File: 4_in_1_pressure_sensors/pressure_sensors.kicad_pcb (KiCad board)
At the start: 4 copper layers, 100 x 100 mm, 73 parts, among them J1 Conn_02x04_Odd_Even, J2 Conn_02x07_Odd_Even, U1 ABPDANT060MGAA5, U1 ABPDJJ001PDSA3, U1 MPX5100AP, U2 LM358

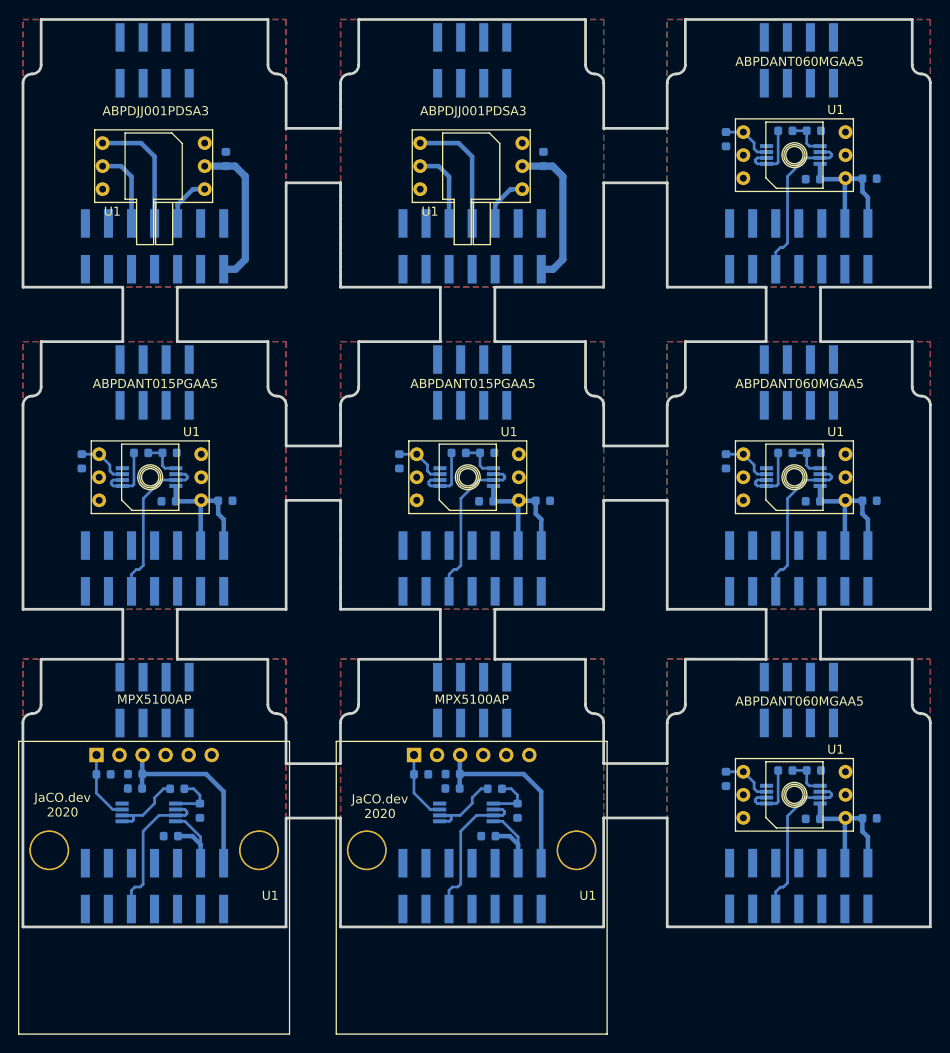
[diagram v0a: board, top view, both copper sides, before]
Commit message: Added mouse bites for pressure sensors PCB
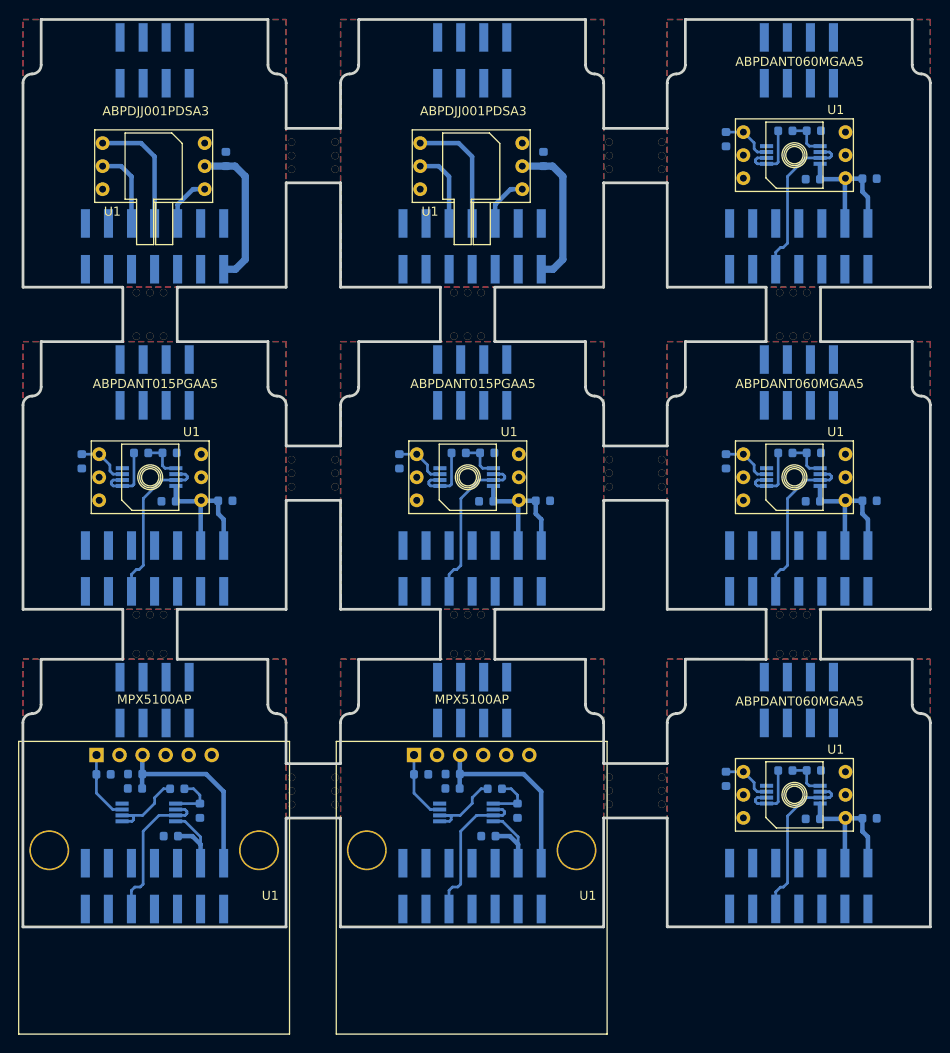
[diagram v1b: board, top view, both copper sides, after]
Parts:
- added ?: SolderWirePad_1x01_Drill0.8mm, Connector_Wire:SolderWirePad_1x01_Drill0.8mm, F.Cu at (204.6, 125.0)
- added ?: SolderWirePad_1x01_Drill0.8mm, Connector_Wire:SolderWirePad_1x01_Drill0.8mm, F.Cu at (210.4, 90.0)
- added ?: SolderWirePad_1x01_Drill0.8mm, Connector_Wire:SolderWirePad_1x01_Drill0.8mm, F.Cu at (204.6, 91.5)
- added ?: SolderWirePad_1x01_Drill0.8mm, Connector_Wire:SolderWirePad_1x01_Drill0.8mm, F.Cu at (204.6, 88.5)
- added ?: SolderWirePad_1x01_Drill0.8mm, Connector_Wire:SolderWirePad_1x01_Drill0.8mm, F.Cu at (210.4, 55.0)
- added ?: SolderWirePad_1x01_Drill0.8mm, Connector_Wire:SolderWirePad_1x01_Drill0.8mm, F.Cu at (204.6, 53.5)
- added ?: SolderWirePad_1x01_Drill0.8mm, Connector_Wire:SolderWirePad_1x01_Drill0.8mm, F.Cu at (210.4, 56.5)
- added ?: SolderWirePad_1x01_Drill0.8mm, Connector_Wire:SolderWirePad_1x01_Drill0.8mm, F.Cu at (204.6, 55.0)
- added ?: SolderWirePad_1x01_Drill0.8mm, Connector_Wire:SolderWirePad_1x01_Drill0.8mm, F.Cu at (210.4, 53.5)
- added ?: SolderWirePad_1x01_Drill0.8mm, Connector_Wire:SolderWirePad_1x01_Drill0.8mm, F.Cu at (204.6, 56.5)
- added ?: SolderWirePad_1x01_Drill0.8mm, Connector_Wire:SolderWirePad_1x01_Drill0.8mm, F.Cu at (174.4, 125.0)
- added ?: SolderWirePad_1x01_Drill0.8mm, Connector_Wire:SolderWirePad_1x01_Drill0.8mm, F.Cu at (210.4, 126.5)
- added ?: SolderWirePad_1x01_Drill0.8mm, Connector_Wire:SolderWirePad_1x01_Drill0.8mm, F.Cu at (169.6, 123.5)
- added ?: SolderWirePad_1x01_Drill0.8mm, Connector_Wire:SolderWirePad_1x01_Drill0.8mm, F.Cu at (174.4, 126.5)
- added ?: SolderWirePad_1x01_Drill0.8mm, Connector_Wire:SolderWirePad_1x01_Drill0.8mm, F.Cu at (169.6, 125.0)
- added ?: SolderWirePad_1x01_Drill0.8mm, Connector_Wire:SolderWirePad_1x01_Drill0.8mm, F.Cu at (174.4, 123.5)
- added ?: SolderWirePad_1x01_Drill0.8mm, Connector_Wire:SolderWirePad_1x01_Drill0.8mm, F.Cu at (169.6, 126.5)
- added ?: SolderWirePad_1x01_Drill0.8mm, Connector_Wire:SolderWirePad_1x01_Drill0.8mm, F.Cu at (174.4, 90.0)
- added ?: SolderWirePad_1x01_Drill0.8mm, Connector_Wire:SolderWirePad_1x01_Drill0.8mm, F.Cu at (169.6, 88.5)
- added ?: SolderWirePad_1x01_Drill0.8mm, Connector_Wire:SolderWirePad_1x01_Drill0.8mm, F.Cu at (174.4, 91.5)
- added ?: SolderWirePad_1x01_Drill0.8mm, Connector_Wire:SolderWirePad_1x01_Drill0.8mm, F.Cu at (169.6, 90.0)
- added ?: SolderWirePad_1x01_Drill0.8mm, Connector_Wire:SolderWirePad_1x01_Drill0.8mm, F.Cu at (174.4, 88.5)
- added ?: SolderWirePad_1x01_Drill0.8mm, Connector_Wire:SolderWirePad_1x01_Drill0.8mm, F.Cu at (210.4, 123.5)
- added ?: SolderWirePad_1x01_Drill0.8mm, Connector_Wire:SolderWirePad_1x01_Drill0.8mm, F.Cu at (169.6, 91.5)
- added ?: SolderWirePad_1x01_Drill0.8mm, Connector_Wire:SolderWirePad_1x01_Drill0.8mm, F.Cu at (174.4, 55.0)
- added ?: SolderWirePad_1x01_Drill0.8mm, Connector_Wire:SolderWirePad_1x01_Drill0.8mm, F.Cu at (169.6, 53.5)
- added ?: SolderWirePad_1x01_Drill0.8mm, Connector_Wire:SolderWirePad_1x01_Drill0.8mm, F.Cu at (174.4, 56.5)
- added ?: SolderWirePad_1x01_Drill0.8mm, Connector_Wire:SolderWirePad_1x01_Drill0.8mm, F.Cu at (169.6, 55.0)
- added ?: SolderWirePad_1x01_Drill0.8mm, Connector_Wire:SolderWirePad_1x01_Drill0.8mm, F.Cu at (174.4, 53.5)
- added ?: SolderWirePad_1x01_Drill0.8mm, Connector_Wire:SolderWirePad_1x01_Drill0.8mm, F.Cu at (169.6, 56.5)
- added ?: SolderWirePad_1x01_Drill0.8mm, Connector_Wire:SolderWirePad_1x01_Drill0.8mm, F.Cu at (224.9, 74.9)
- added ?: SolderWirePad_1x01_Drill0.8mm, Connector_Wire:SolderWirePad_1x01_Drill0.8mm, F.Cu at (226.4, 70.1)
- added ?: SolderWirePad_1x01_Drill0.8mm, Connector_Wire:SolderWirePad_1x01_Drill0.8mm, F.Cu at (223.4, 74.9)
- added ?: SolderWirePad_1x01_Drill0.8mm, Connector_Wire:SolderWirePad_1x01_Drill0.8mm, F.Cu at (210.4, 125.0)
- added ?: SolderWirePad_1x01_Drill0.8mm, Connector_Wire:SolderWirePad_1x01_Drill0.8mm, F.Cu at (224.9, 70.1)
- added ?: SolderWirePad_1x01_Drill0.8mm, Connector_Wire:SolderWirePad_1x01_Drill0.8mm, F.Cu at (226.4, 74.9)
- added ?: SolderWirePad_1x01_Drill0.8mm, Connector_Wire:SolderWirePad_1x01_Drill0.8mm, F.Cu at (223.4, 70.1)
- added ?: SolderWirePad_1x01_Drill0.8mm, Connector_Wire:SolderWirePad_1x01_Drill0.8mm, F.Cu at (189.0, 74.9)
- added ?: SolderWirePad_1x01_Drill0.8mm, Connector_Wire:SolderWirePad_1x01_Drill0.8mm, F.Cu at (190.5, 70.1)
- added ?: SolderWirePad_1x01_Drill0.8mm, Connector_Wire:SolderWirePad_1x01_Drill0.8mm, F.Cu at (187.5, 74.9)
- added ?: SolderWirePad_1x01_Drill0.8mm, Connector_Wire:SolderWirePad_1x01_Drill0.8mm, F.Cu at (189.0, 70.1)
- added ?: SolderWirePad_1x01_Drill0.8mm, Connector_Wire:SolderWirePad_1x01_Drill0.8mm, F.Cu at (190.5, 74.9)
- added ?: SolderWirePad_1x01_Drill0.8mm, Connector_Wire:SolderWirePad_1x01_Drill0.8mm, F.Cu at (187.5, 70.1)
- added ?: SolderWirePad_1x01_Drill0.8mm, Connector_Wire:SolderWirePad_1x01_Drill0.8mm, F.Cu at (152.5, 74.9)
- added ?: SolderWirePad_1x01_Drill0.8mm, Connector_Wire:SolderWirePad_1x01_Drill0.8mm, F.Cu at (204.6, 126.5)
- added ?: SolderWirePad_1x01_Drill0.8mm, Connector_Wire:SolderWirePad_1x01_Drill0.8mm, F.Cu at (154.0, 74.9)
- added ?: SolderWirePad_1x01_Drill0.8mm, Connector_Wire:SolderWirePad_1x01_Drill0.8mm, F.Cu at (155.5, 74.9)
- added ?: SolderWirePad_1x01_Drill0.8mm, Connector_Wire:SolderWirePad_1x01_Drill0.8mm, F.Cu at (154.0, 70.1)
- added ?: SolderWirePad_1x01_Drill0.8mm, Connector_Wire:SolderWirePad_1x01_Drill0.8mm, F.Cu at (152.5, 70.1)
- added ?: SolderWirePad_1x01_Drill0.8mm, Connector_Wire:SolderWirePad_1x01_Drill0.8mm, F.Cu at (155.5, 70.1)
- added ?: SolderWirePad_1x01_Drill0.8mm, Connector_Wire:SolderWirePad_1x01_Drill0.8mm, F.Cu at (152.5, 109.9)
- added ?: SolderWirePad_1x01_Drill0.8mm, Connector_Wire:SolderWirePad_1x01_Drill0.8mm, F.Cu at (154.0, 109.9)
- added ?: SolderWirePad_1x01_Drill0.8mm, Connector_Wire:SolderWirePad_1x01_Drill0.8mm, F.Cu at (155.5, 109.9)
- added ?: SolderWirePad_1x01_Drill0.8mm, Connector_Wire:SolderWirePad_1x01_Drill0.8mm, F.Cu at (154.0, 105.6)
- added ?: SolderWirePad_1x01_Drill0.8mm, Connector_Wire:SolderWirePad_1x01_Drill0.8mm, F.Cu at (152.5, 105.6)
- added ?: SolderWirePad_1x01_Drill0.8mm, Connector_Wire:SolderWirePad_1x01_Drill0.8mm, F.Cu at (204.6, 123.5)
- added ?: SolderWirePad_1x01_Drill0.8mm, Connector_Wire:SolderWirePad_1x01_Drill0.8mm, F.Cu at (155.5, 105.6)
- added ?: SolderWirePad_1x01_Drill0.8mm, Connector_Wire:SolderWirePad_1x01_Drill0.8mm, F.Cu at (187.5, 109.9)
- added ?: SolderWirePad_1x01_Drill0.8mm, Connector_Wire:SolderWirePad_1x01_Drill0.8mm, F.Cu at (189.0, 109.9)
- added ?: SolderWirePad_1x01_Drill0.8mm, Connector_Wire:SolderWirePad_1x01_Drill0.8mm, F.Cu at (190.5, 109.9)
- added ?: SolderWirePad_1x01_Drill0.8mm, Connector_Wire:SolderWirePad_1x01_Drill0.8mm, F.Cu at (189.0, 105.6)
- added ?: SolderWirePad_1x01_Drill0.8mm, Connector_Wire:SolderWirePad_1x01_Drill0.8mm, F.Cu at (187.5, 105.6)
- added ?: SolderWirePad_1x01_Drill0.8mm, Connector_Wire:SolderWirePad_1x01_Drill0.8mm, F.Cu at (190.5, 105.6)
- added ?: SolderWirePad_1x01_Drill0.8mm, Connector_Wire:SolderWirePad_1x01_Drill0.8mm, F.Cu at (224.9, 109.9)
- added ?: SolderWirePad_1x01_Drill0.8mm, Connector_Wire:SolderWirePad_1x01_Drill0.8mm, F.Cu at (223.4, 109.9)
- added ?: SolderWirePad_1x01_Drill0.8mm, Connector_Wire:SolderWirePad_1x01_Drill0.8mm, F.Cu at (226.4, 109.9)
- added ?: SolderWirePad_1x01_Drill0.8mm, Connector_Wire:SolderWirePad_1x01_Drill0.8mm, F.Cu at (204.6, 90.0)
- added ?: SolderWirePad_1x01_Drill0.8mm, Connector_Wire:SolderWirePad_1x01_Drill0.8mm, F.Cu at (223.4, 105.6)
- added ?: SolderWirePad_1x01_Drill0.8mm, Connector_Wire:SolderWirePad_1x01_Drill0.8mm, F.Cu at (224.9, 105.6)
- added ?: SolderWirePad_1x01_Drill0.8mm, Connector_Wire:SolderWirePad_1x01_Drill0.8mm, F.Cu at (226.4, 105.6)
- added ?: SolderWirePad_1x01_Drill0.8mm, Connector_Wire:SolderWirePad_1x01_Drill0.8mm, F.Cu at (210.4, 91.5)
- added ?: SolderWirePad_1x01_Drill0.8mm, Connector_Wire:SolderWirePad_1x01_Drill0.8mm, F.Cu at (210.4, 88.5)
